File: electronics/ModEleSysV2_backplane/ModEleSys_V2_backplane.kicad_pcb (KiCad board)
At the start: 2 copper layers, 90 x 98 mm, 40 parts, among them J13 Conn_01x03, J15 Conn_01x03, J5 Conn_01x03, J6 Conn_01x03, J7 Conn_01x03, J8 Conn_01x03, SW1 switch_DPDT, SW2 switch_DPDT

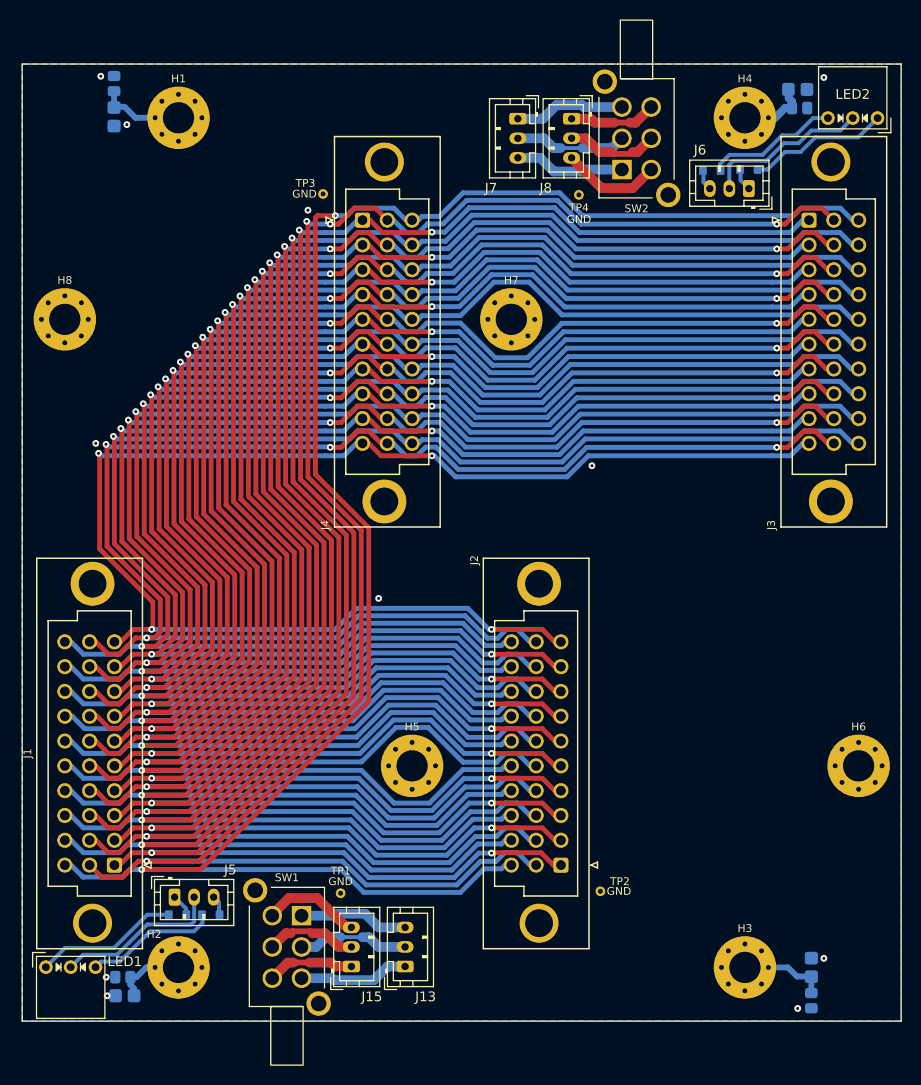
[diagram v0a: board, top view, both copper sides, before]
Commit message: changed power on/off connector on backplane
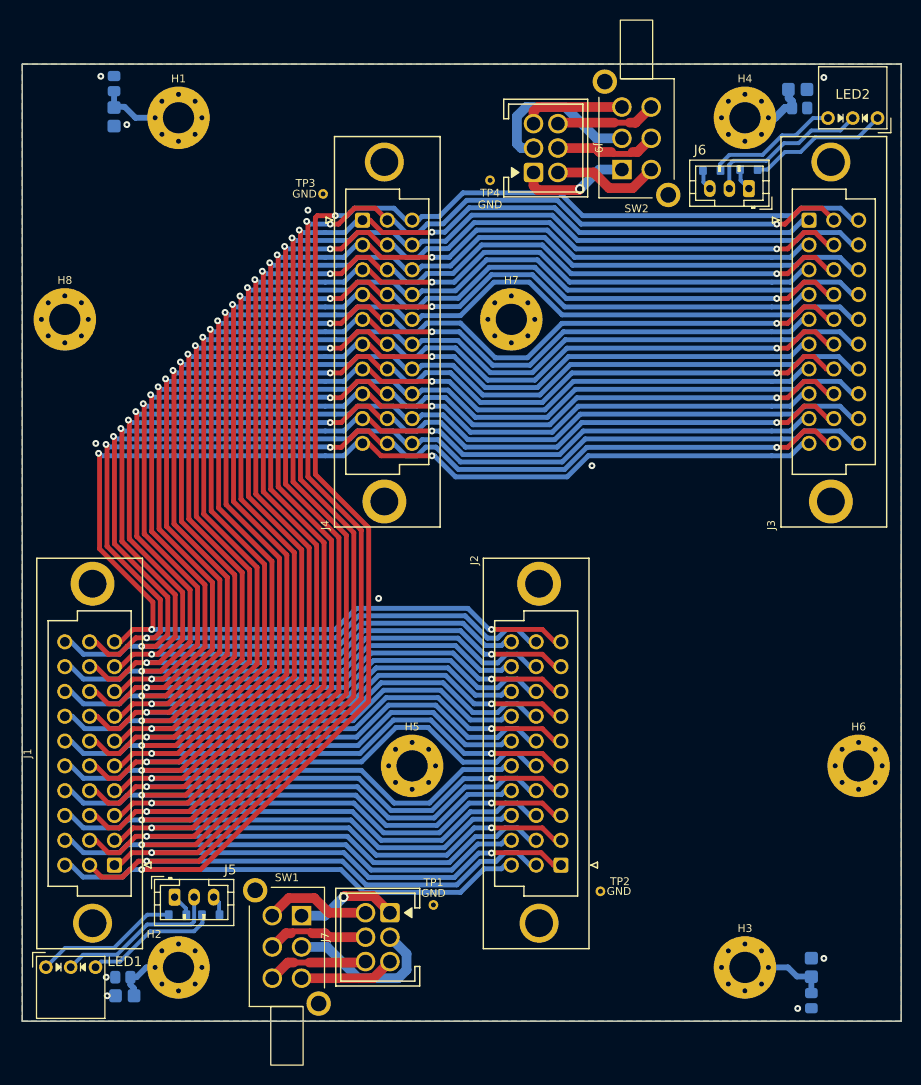
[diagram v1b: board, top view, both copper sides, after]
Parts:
- removed J13, J15, J8: Conn_01x03, Connector_JST:JST_PH_B3B-PH-K_1x03_P2.00mm_Vertical
- added J9: Conn_02x03_Odd_Even, SquantorConnectors:DLL-XHY-6A, F.Cu at (173.7, 48.5)
- J7: value Conn_01x03 -> Conn_02x03_Odd_Even; footprint Connector_JST:JST_PH_B3B-PH-K_1x03_P2.00mm_Vertical -> SquantorConnectors:DLL-XHY-6A
- moved J7 85.0 mm to (156.5, 129.3), turned to 90 degrees
- moved TP1 9.58 mm to (162.2, 126.0)
- moved TP4 9.22 mm to (168.0, 51.8)
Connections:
- SW1 pad 1: Net-(J13-Pin_3) -> Net-(J7-Pin_1)
- SW1 pad 2: Net-(J13-Pin_2) -> Net-(J7-Pin_3)
- SW1 pad 3: Net-(J13-Pin_1) -> Net-(J7-Pin_5)
- SW1 pad 4: Net-(J15-Pin_1) -> Net-(J7-Pin_6)
- SW1 pad 5: Net-(J15-Pin_2) -> Net-(J7-Pin_4)
- SW1 pad 6: Net-(J15-Pin_3) -> Net-(J7-Pin_2)
- SW2 pad 1: Net-(J7-Pin_3) -> Net-(J9-Pin_1)
- SW2 pad 2: Net-(J7-Pin_2) -> Net-(J9-Pin_3)
- SW2 pad 3: Net-(J7-Pin_1) -> Net-(J9-Pin_5)
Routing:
- net Net-(J9-Pin_3): track 0.00 -> 17.2 mm
- net Net-(J9-Pin_1): track 0.00 -> 11.5 mm, vias 0 -> 1
- net Net-(J13-Pin_2): track 11.4 -> 0.00 mm
- net Net-(J13-Pin_3): track 11.3 -> 0.00 mm
- net Net-(J13-Pin_1): track 11.3 -> 0.00 mm
- net Net-(J9-Pin_5): track 0.00 -> 10.5 mm
- net Net-(J7-Pin_4): track 0.00 -> 10.5 mm
- net Net-(J7-Pin_6): track 0.00 -> 10.3 mm
- net Net-(J15-Pin_3): track 10.1 -> 0.00 mm
- net Net-(J7-Pin_5): track 0.00 -> 9.75 mm
- net Net-(J15-Pin_2): track 9.43 -> 0.00 mm
- net Net-(J15-Pin_1): track 8.93 -> 0.00 mm
- net Net-(J7-Pin_3): track 11.3 -> 16.5 mm
- net Net-(J9-Pin_6): track 8.98 -> 10.3 mm
- net Net-(J9-Pin_4): track 9.48 -> 10.5 mm
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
